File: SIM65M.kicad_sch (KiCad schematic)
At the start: 20 parts, among them J3 Conn_01x10_Pin, Q1 AO3400A, Q2 DTC143ZUAT106, Q3 DTC143ZUAT106, U1 SIM65M_C7495025, U2 BWGNSCNX25-25W4, U4 TXS0102DCUR, U5 XC6206P282MR-G

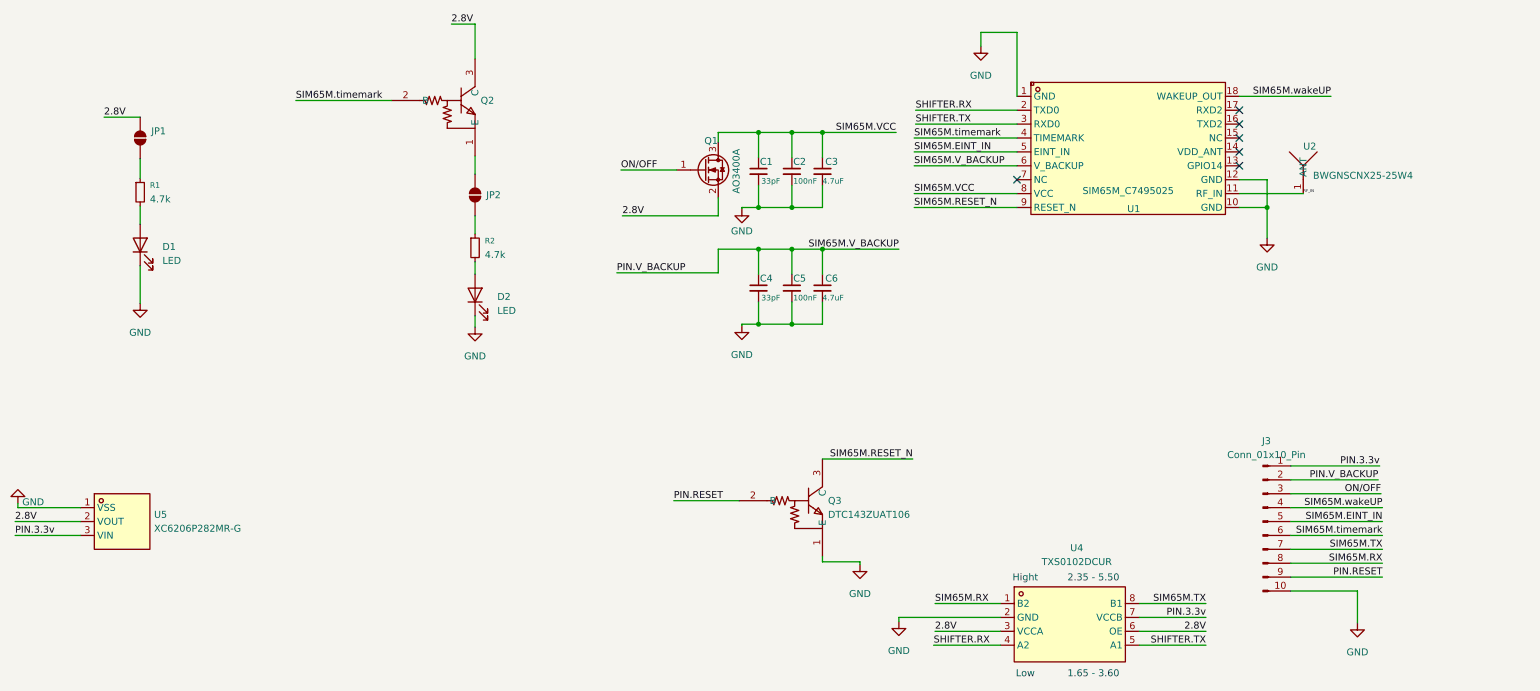
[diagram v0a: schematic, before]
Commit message: agregado UFL
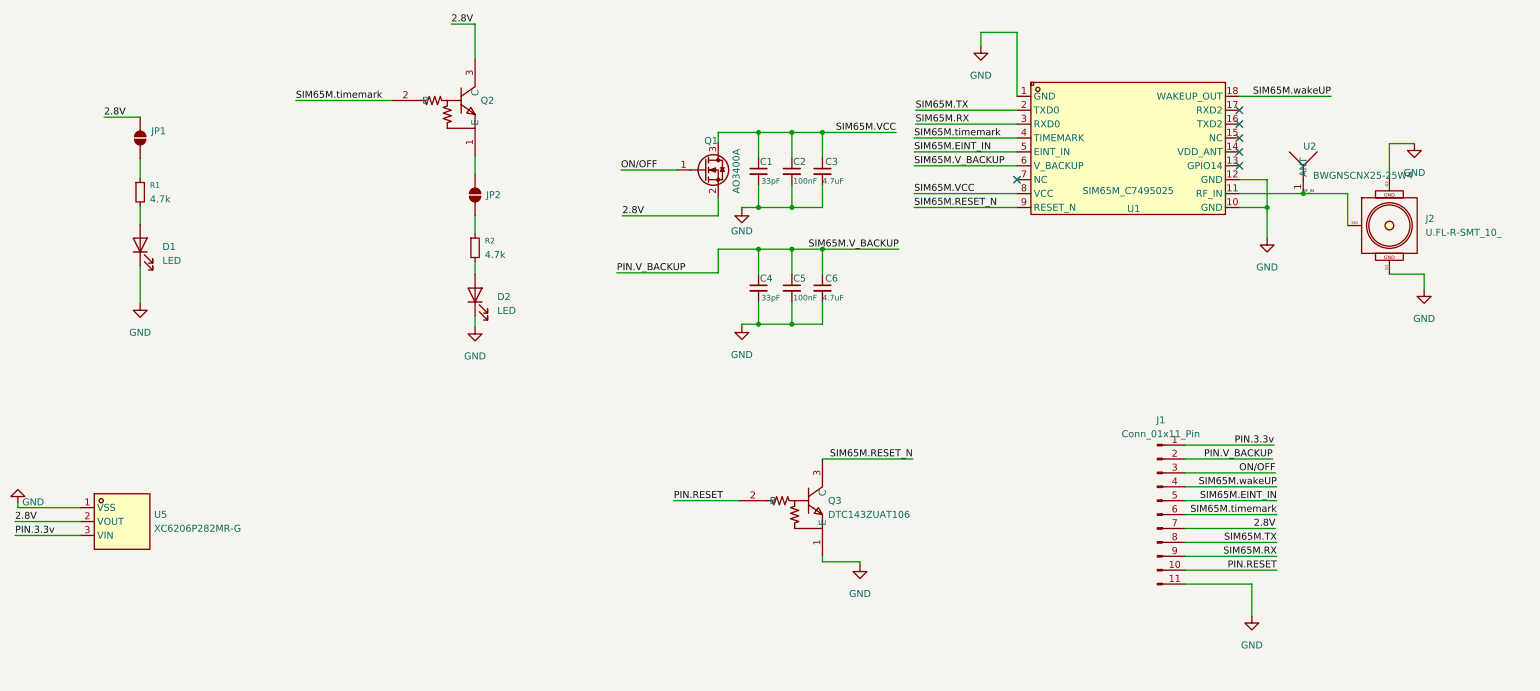
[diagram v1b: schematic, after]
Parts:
- removed J3: Conn_01x10_Pin, Connector_PinHeader_2.54mm:PinHeader_1x10_P2.54mm_Vertical, symbol Connector:Conn_01x10_Pin
- removed U4: TXS0102DCUR, EasyEDA:VSON8_L2.0-W2.3-P0.50-LS3.1-BL, symbol EasyEDA:TXS0102DCUR
- added J1: Conn_01x11_Pin, Connector_PinHeader_2.54mm:PinHeader_1x11_P2.54mm_Vertical, symbol Connector:Conn_01x11_Pin
- added J2: U.FL-R-SMT_10_, Snapeda:U.FL-R-SMT_10_-foot, symbol Snapeda:U.FL-R-SMT_10_
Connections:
- net SHIFTER.RX is gone; now on net SIM65M.TX: U1.2 (TXD0)
- net SHIFTER.TX is gone; now on net SIM65M.RX: U1.3 (RXD0)
- net 2.8V: now also J1.7 (Pin_7)
- net GND: now also J1.11 (Pin_11), J2.G1, J2.G2
- net ON/OFF: now also J1.3 (Pin_3)
- net PIN.3.3v: now also J1.1 (Pin_1)
- net PIN.RESET: now also J1.10 (Pin_10)
- net PIN.V_BACKUP: now also J1.2 (Pin_2)
- net RF_IN: now also J2.SIG
- net SIM65M.EINT_IN: now also J1.5 (Pin_5)
- net SIM65M.RX: now also J1.9 (Pin_9)
- net SIM65M.TX: now also J1.8 (Pin_8)
- net SIM65M.timemark: now also J1.6 (Pin_6)
- net SIM65M.wakeUP: now also J1.4 (Pin_4)
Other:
- note removed: "1.65 - 3.60"
- note removed: "2.35 - 5.50"
- note removed: "Hight"
- note removed: "Low"

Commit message: rediseño etapa RF, agregada bifurcacion para activa/pasiva, mejoras generales en RF
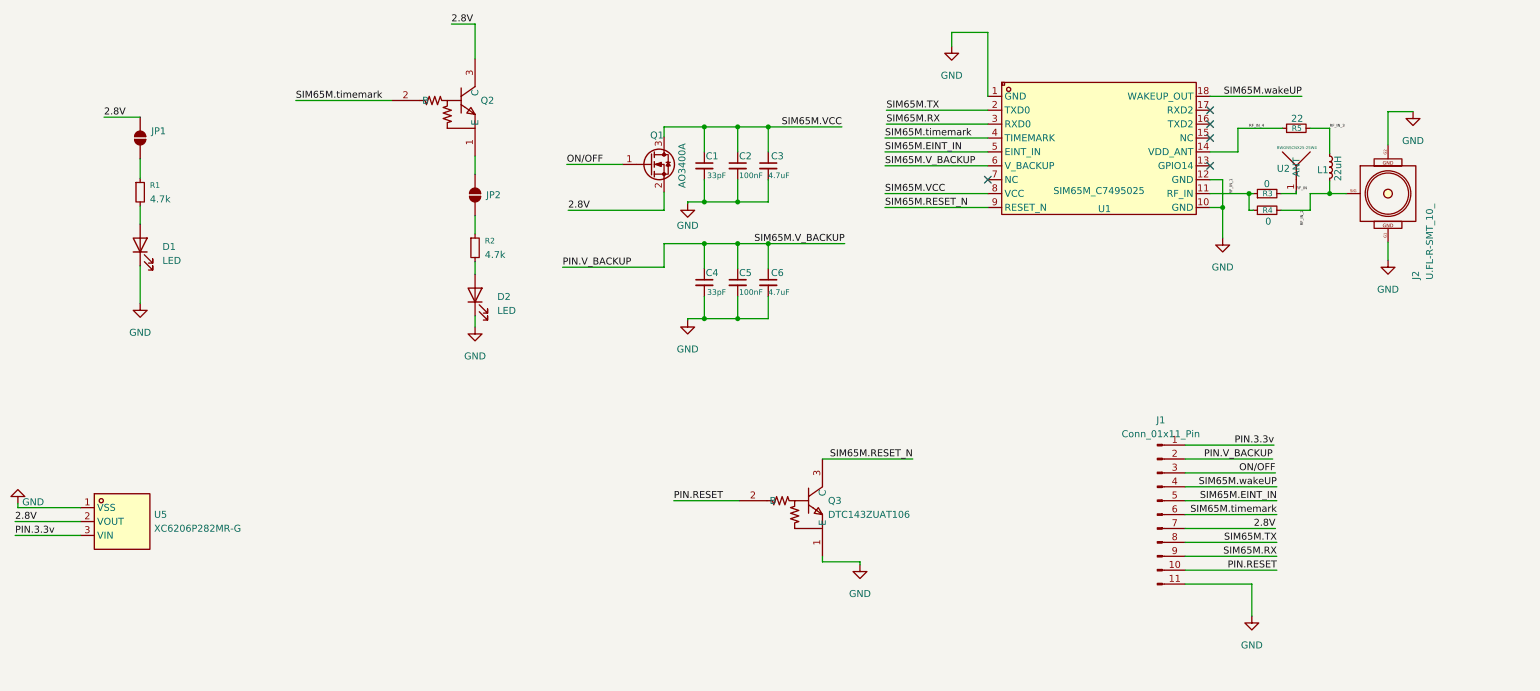
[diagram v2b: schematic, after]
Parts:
- added L1: 22uH, Inductor_SMD:L_0402_1005Metric, symbol Device:L_Small
- added R3, R4: 0, Resistor_SMD:R_0201_0603Metric_Pad0.64x0.40mm_HandSolder, symbol Device:R_Small
- added R5: 22, Resistor_SMD:R_0201_0603Metric_Pad0.64x0.40mm_HandSolder, symbol Device:R_Small
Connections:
- net RF_IN: now also R3.2; no longer J2.SIG, U1.11 (RF_IN)
- net RF_IN_4: now reaches U1.14 (VDD_ANT)
- net RF_IN_4: now also R5.1
- new net RF_IN_1: R3.1, R4.1, U1.11 (RF_IN)
- new net RF_IN_2: J2.SIG, L1.2, R4.2
- new net RF_IN_3: L1.1, R5.2
- no-connect marks 6 -> 5
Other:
- moved on the sheet: C1, C2, C3, C4, C5, C6, J2, Q1, U1, U2
